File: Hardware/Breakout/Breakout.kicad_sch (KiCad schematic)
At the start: 17 parts, among them J1 Conn_Coaxial, U1 TDC7200PWR, U2 BUF602ID, U3 MAX9011EUT+T, U4 MAX7375AXR805+T

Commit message: sanity check commit to make sure changes are saved
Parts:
- added J2: 9v_batt_in, Connector_PinHeader_2.54mm:PinHeader_1x02_P2.54mm_Vertical, symbol Connector_Generic:Conn_01x02
- added TP1, TP2: TestPoint, Connector_PinHeader_2.54mm:PinHeader_1x01_P2.54mm_Vertical, symbol Connector:TestPoint
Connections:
- net +9V: now also J2.2 (Pin_2)
- net GND: now also J2.1 (Pin_1)
- net REFCLK: now also TP2.1
- net STOP: now also TP1.1
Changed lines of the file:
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@@
 (kicad_sch (version 20230121) (generator eeschema)
   (paper "A4")
+  (junction (at 182.88 100.33) (diameter 0) (color 0 0 0 0)
+  )
   (junction (at 200.66 34.29) (diameter 0) (color 0 0 0 0)
   )
@@
   )
   (junction (at 246.38 95.25) (diameter 0) (color 0 0 0 0)
+  )
+  (junction (at 105.41 128.27) (diameter 0) (color 0 0 0 0)
   )
   (junction (at 262.89 34.29) (diameter 0) (color 0 0 0 0)
@@
   (no_connect (at 172.72 125.73))
   (no_connect (at 93.98 133.35))
+  (wire (pts (xy 182.88 91.44) (xy 182.88 100.33))
+    (stroke (width 0) (type default))
+  )
   (wire (pts (xy 90.17 21.59) (xy 90.17 31.75))
     (stroke (width 0) (type default))
@@
     (stroke (width 0) (type default))
   )
+  (wire (pts (xy 104.14 17.78) (xy 104.14 22.86))
+    (stroke (width 0) (type default))
+  )
   (wire (pts (xy 30.48 62.23) (xy 34.29 62.23))
     (stroke (width 0) (type default))
@@
     (stroke (width 0) (type default))
   )
-  (wire (pts (xy 179.07 100.33) (xy 187.96 100.33))
+  (wire (pts (xy 179.07 100.33) (xy 182.88 100.33))
     (stroke (width 0) (type default))
   )
@@
     (stroke (width 0) (type default))
   )
+  (wire (pts (xy 105.41 128.27) (xy 110.49 128.27))
+    (stroke (width 0) (type default))
+  )
   (wire (pts (xy 30.48 170.18) (xy 30.48 172.72))
     (stroke (width 0) (type default))
@@
     (stroke (width 0) (type default))
   )
+  (wire (pts (xy 105.41 128.27) (xy 105.41 134.62))
+    (stroke (width 0) (type default))
+  )
   (wire (pts (xy 106.68 97.79) (xy 113.03 97.79))
     (stroke (width 0) (type default))
@@
     (stroke (width 0) (type default))
   )
-  (wire (pts (xy 93.98 128.27) (xy 96.52 128.27))
+  (wire (pts (xy 93.98 128.27) (xy 105.41 128.27))
     (stroke (width 0) (type default))
   )
@@
     (stroke (width 0) (type default))
   )
+  (wire (pts (xy 104.14 22.86) (xy 106.68 22.86))
+    (stroke (width 0) (type default))
+  )
   (wire (pts (xy 200.66 34.29) (xy 204.47 34.29))
     (stroke (width 0) (type default))
@@
     (stroke (width 0) (type default))
   )
+  (wire (pts (xy 109.22 17.78) (xy 109.22 22.86))
+    (stroke (width 0) (type default))
+  )
   (wire (pts (xy 137.16 107.95) (xy 137.16 118.11))
     (stroke (width 0) (type default))
@@
   )
   (wire (pts (xy 243.84 100.33) (xy 246.38 100.33))
+    (stroke (width 0) (type default))
+  )
+  (wire (pts (xy 182.88 100.33) (xy 187.96 100.33))
     (stroke (width 0) (type default))
   )
@@
     )
   )
-  (global_label "REFCLK" (shape input) (at 96.52 128.27 0) (fields_autoplaced)
+  (global_label "REFCLK" (shape input) (at 110.49 128.27 0) (fields_autoplaced)
     (effects (font (size 1.27 1.27)) (justify left))
-    (property "Intersheetrefs" "${INTERSHEET_REFS}" (at 106.5015 128.27 0)
+    (property "Intersheetrefs" "${INTERSHEET_REFS}" (at 120.4715 128.27 0)
       (effects (font (size 1.27 1.27)) (justify left) hide)
     )
@@
     )
   )
+  (symbol (lib_id "Connector:TestPoint") (at 182.88 91.44 0) (unit 1)
+    (in_bom yes) (on_board yes) (dnp no) (fields_autoplaced)
+    (property "Reference" "TP1" (at 185.42 87.503 0)
+      (effects (font (size 1.27 1.27)) (justify left))
+    )
+    (property "Value" "TestPoint" (at 185.42 90.043 0)
+      (effects (font (size 1.27 1.27)) (justify left))
+    )
+    (property "Footprint" "Connector_PinHeader_2.54mm:PinHeader_1x01_P2.54mm_Vertical" (at 187.96 91.44 0)
+      (effects (font (size 1.27 1.27)) hide)
+    )
+    (property "Datasheet" "~" (at 187.96 91.44 0)
+      (effects (font (size 1.27 1.27)) hide)
+    )
+    (pin "1")
+    (instances
+      (project "Breakout"
+        (path "/c2ef38f9-0f55-4b19-9130-d81b036a0cd1"
+          (reference "TP1") (unit 1)
+        )
+      )
+    )
+  )
   (symbol (lib_id "power:+3.3V") (at 129.54 52.07 0) (unit 1)
     (in_bom yes) (on_board yes) (dnp no) (fields_autoplaced)
@@
     )
   )
+  (symbol (lib_id "power:+9V") (at 104.14 17.78 0) (unit 1)
+    (in_bom yes) (on_board yes) (dnp no) (fields_autoplaced)
+    (property "Reference" "#PWR025" (at 104.14 21.59 0)
+      (effects (font (size 1.27 1.27)) hide)
+    )
+    (property "Value" "+9V" (at 104.14 12.7 0)
+      (effects (font (size 1.27 1.27)))
+    )
+    (property "Footprint" "" (at 104.14 17.78 0)
+      (effects (font (size 1.27 1.27)) hide)
+    )
+    (property "Datasheet" "" (at 104.14 17.78 0)
+      (effects (font (size 1.27 1.27)) hide)
+    )
+    (pin "1")
+    (instances
+      (project "Breakout"
+        (path "/c2ef38f9-0f55-4b19-9130-d81b036a0cd1"
+          (reference "#PWR025") (unit 1)
+        )
+      )
+    )
+  )
+  (symbol (lib_id "power:GND") (at 109.22 17.78 180) (unit 1)
+    (in_bom yes) (on_board yes) (dnp no) (fields_autoplaced)
+    (property "Reference" "#PWR08" (at 109.22 11.43 0)
+      (effects (font (size 1.27 1.27)) hide)
+    )
+    (property "Value" "GND" (at 109.22 12.7 0)
+      (effects (font (size 1.27 1.27)))
+    )
+    (property "Footprint" "" (at 109.22 17.78 0)
+      (effects (font (size 1.27 1.27)) hide)
+    )
+    (property "Datasheet" "" (at 109.22 17.78 0)
+      (effects (font (size 1.27 1.27)) hide)
+    )
+    (pin "1")
+    (instances
+      (project "TDR"
+        (path "/1d71c98b-8f12-499e-a653-7a49d25d3cb1"
+          (reference "#PWR08") (unit 1)
+        )
+      )
+      (project "Breakout"
+        (path "/c2ef38f9-0f55-4b19-9130-d81b036a0cd1"
+          (reference "#PWR026") (unit 1)
+        )
+      )
+    )
+  )
   (symbol (lib_id "power:GND") (at 204.47 48.26 0) (unit 1)
     (in_bom yes) (on_board yes) (dnp no) (fields_autoplaced)
@@
         (path "/c2ef38f9-0f55-4b19-9130-d81b036a0cd1"
           (reference "C5") (unit 1)
+        )
+      )
+    )
+  )
+  (symbol (lib_id "Connector_Generic:Conn_01x02") (at 109.22 27.94 270) (unit 1)
+    (in_bom yes) (on_board yes) (dnp no) (fields_autoplaced)
+    (property "Reference" "J2" (at 111.76 27.305 90)
+      (effects (font (size 1.27 1.27)) (justify left))
+    )
+    (property "Value" "9v_batt_in" (at 111.76 29.845 90)
+      (effects (font (size 1.27 1.27)) (justify left))
+    )
+    (property "Footprint" "Connector_PinHeader_2.54mm:PinHeader_1x02_P2.54mm_Vertical" (at 109.22 27.94 0)
+      (effects (font (size 1.27 1.27)) hide)
+    )
+    (property "Datasheet" "~" (at 109.22 27.94 0)
+      (effects (font (size 1.27 1.27)) hide)
+    )
+    (pin "1")
+    (pin "2")
+    (instances
+      (project "Breakout"
+        (path "/c2ef38f9-0f55-4b19-9130-d81b036a0cd1"
+          (reference "J2") (unit 1)
         )
       )
@@
         )
       )
+    )
+  )
+  (symbol (lib_id "Connector:TestPoint") (at 105.41 134.62 180) (unit 1)
+    (in_bom yes) (on_board yes) (dnp no) (fields_autoplaced)
+    (property "Reference" "TP2" (at 107.95 137.287 0)
+      (effects (font (size 1.27 1.27)) (justify right))
+    )
+    (property "Value" "TestPoint" (at 107.95 139.827 0)
+      (effects (font (size 1.27 1.27)) (justify right))
+    )
+    (property "Footprint" "Connector_PinHeader_2.54mm:PinHeader_1x01_P2.54mm_Vertical" (at 100.33 134.62 0)
+      (effects (font (size 1.27 1.27)) hide)
+    )
+    (property "Datasheet" "~" (at 100.33 134.62 0)
+      (effects (font (size 1.27 1.27)) hide)
+    )
+    (pin "1")
+    (instances
+      (project "Breakout"
+        (path "/c2ef38f9-0f55-4b19-9130-d81b036a0cd1"
+          (reference "TP2") (unit 1)
+        )
+      )

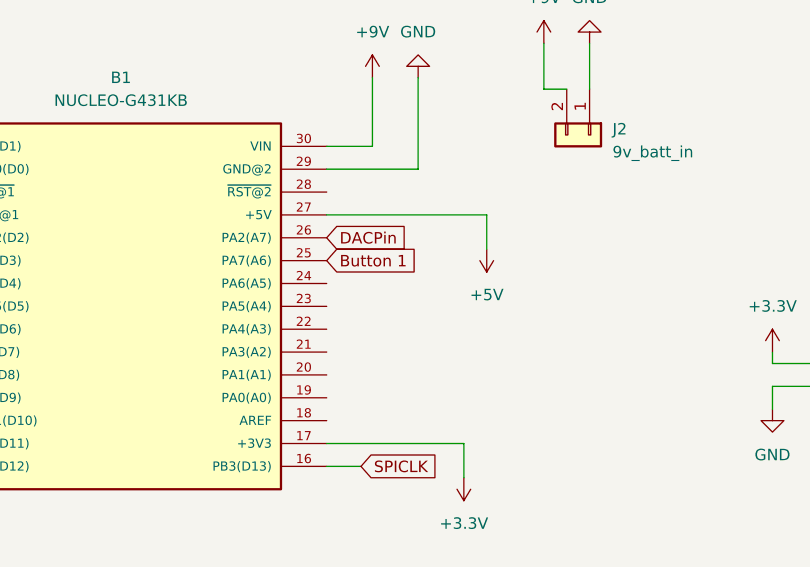
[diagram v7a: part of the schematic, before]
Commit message: fixed DAC pin
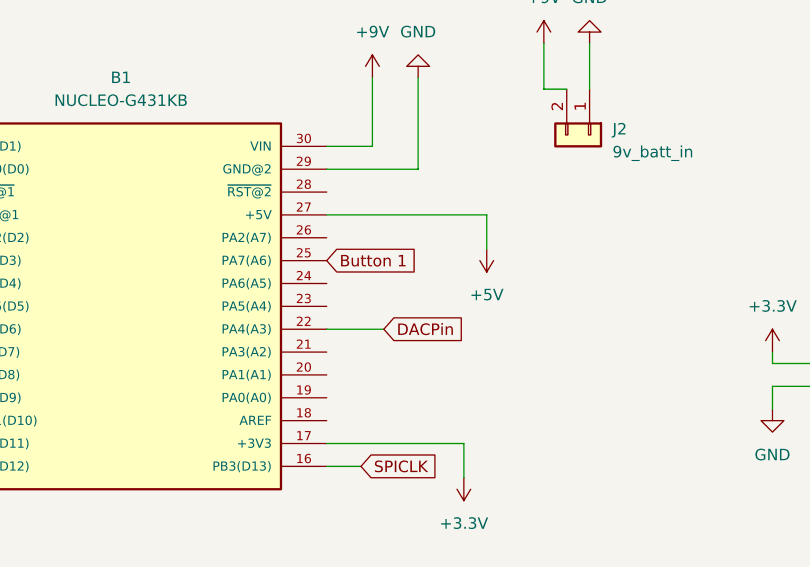
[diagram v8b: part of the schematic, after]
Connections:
- net DACPin: now also B1.22 (PA4(A3)); no longer B1.26 (PA2(A7))
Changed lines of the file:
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@@
+    (stroke (width 0) (type default))
+  )
+  (wire (pts (xy 80.01 49.53) (xy 86.36 49.53))
     (stroke (width 0) (type default))
   )
@@
     )
   )
-  (global_label "DACPin" (shape input) (at 80.01 39.37 0) (fields_autoplaced)
-    (effects (font (size 1.27 1.27)) (justify left))
-    (property "Intersheetrefs" "${INTERSHEET_REFS}" (at 89.5682 39.37 0)
-      (effects (font (size 1.27 1.27)) (justify left) hide)
-    )
+  (global_label "DACPin" (shape input) (at 86.36 49.53 0) (fields_autoplaced)
+    (effects (font (size 1.27 1.27)) (justify left))
+    (property "Intersheetrefs" "${INTERSHEET_REFS}" (at 95.9182 49.53 0)
+      (effects (font (size 1.27 1.27)) (justify left) hide)
+    )
